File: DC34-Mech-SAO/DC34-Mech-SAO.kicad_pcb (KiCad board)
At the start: 2 copper layers, 26.8 x 37 mm, 15 parts, among them J1 Conn_01x06_Male, U1 ATTINY817-MN

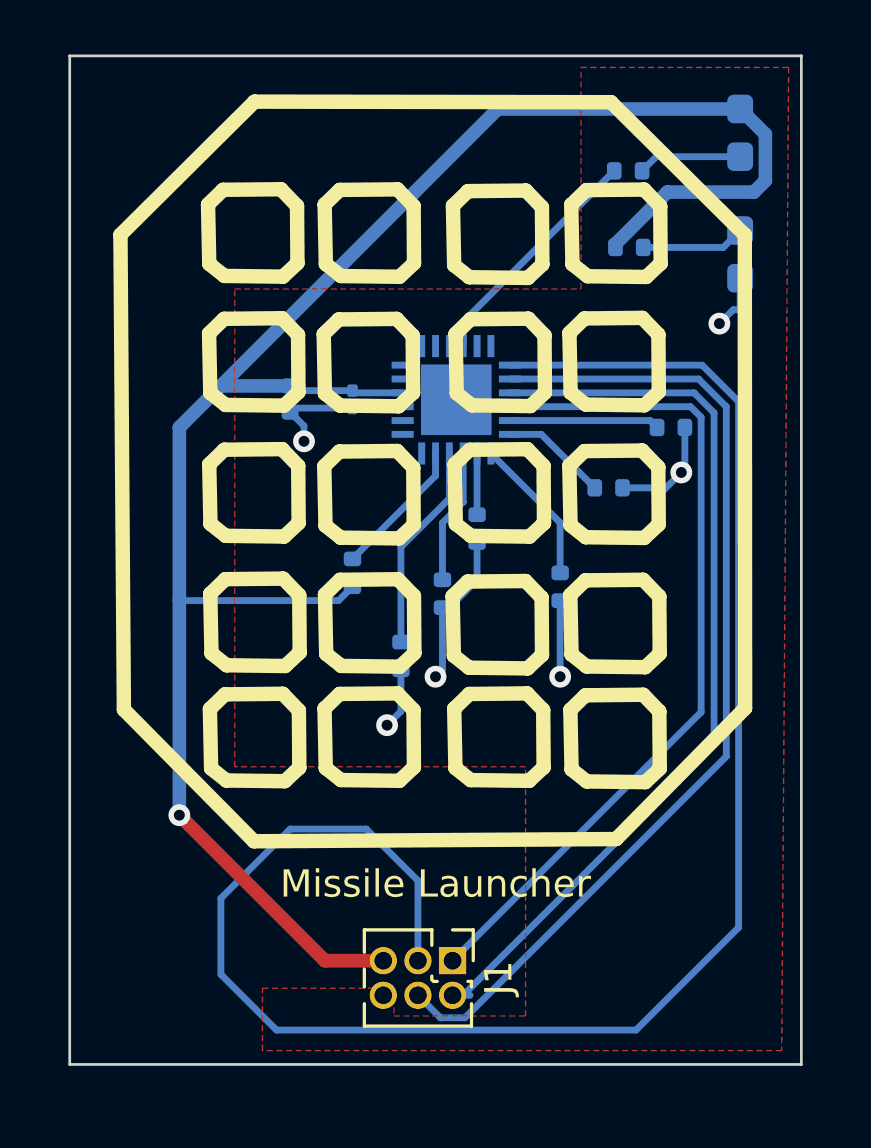
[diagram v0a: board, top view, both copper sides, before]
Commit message: Using ATTiny 816.
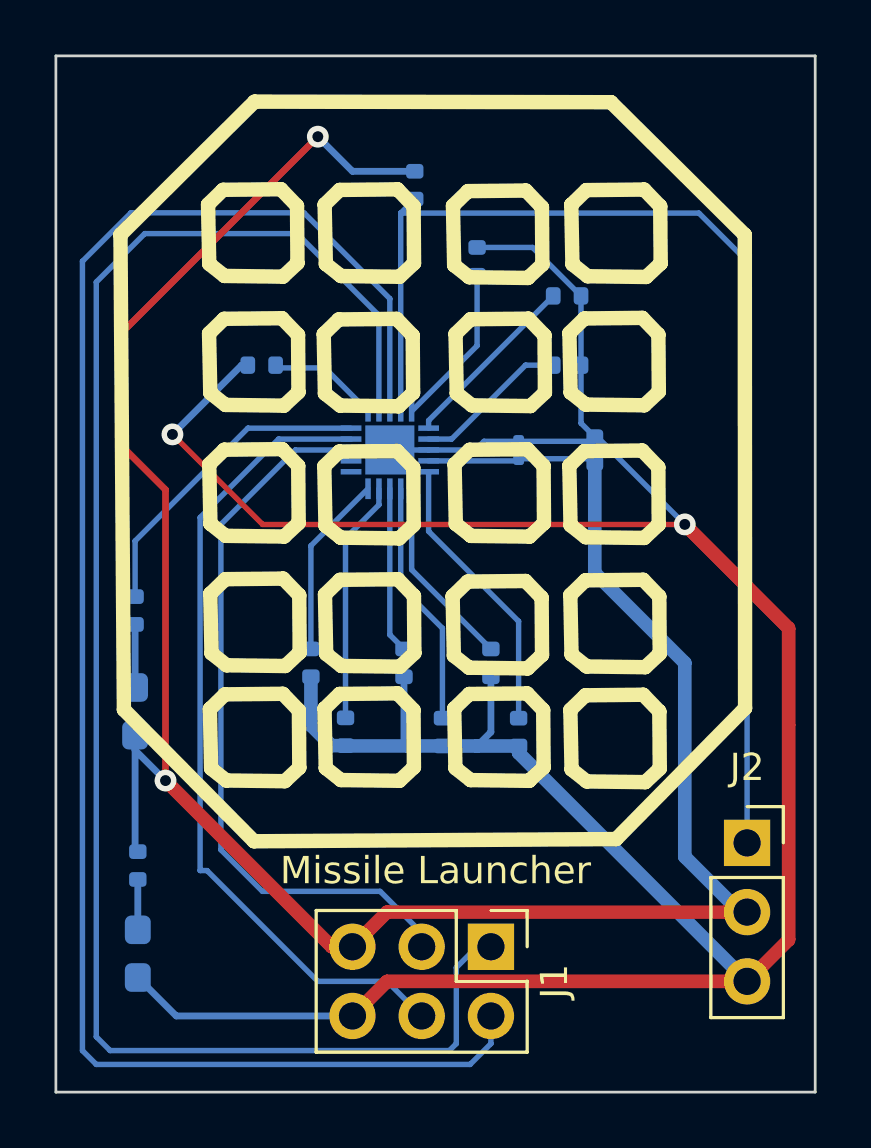
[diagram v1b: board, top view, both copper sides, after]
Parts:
- added J2: Conn_01x03_Male, Connector_PinSocket_2.54mm:PinSocket_1x03_P2.54mm_Vertical, F.Cu at (156.2, 90.9)
- added R11: 10k, Resistor_SMD:R_0402_1005Metric, B.Cu at (146.3, 69.6)
- added R12: 10k, Resistor_SMD:R_0402_1005Metric, B.Cu at (149.6, 70.9)
- added R13: 10k, Resistor_SMD:R_0402_1005Metric, B.Cu at (149.6, 73.4)
- added R7: 10k, Resistor_SMD:R_0402_1005Metric, B.Cu at (143.6, 84.3)
- J1: footprint Connector_PinHeader_1.27mm:PinHeader_2x03_P1.27mm_Vertical -> Connector_PinHeader_2.54mm:PinHeader_2x03_P2.54mm_Vertical
- U1: value ATTINY817-MN -> ATtiny816-M; footprint ATTINY817:QFN24_4X4MC_MCH -> ATTINY816:VQFN20_3X3_MCH
- moved D2 33.9 mm to (133.9, 95.0)
- moved D1 30.7 mm to (133.8, 86.1), turned to -90 degrees
- moved R2 29.0 mm to (133.9, 91.8), turned to -90 degrees
- moved R1 24.2 mm to (133.8, 82.4), turned to 90 degrees
- moved R10 15.2 mm to (138.4, 73.4), turned to 180 degrees
- moved R3 14.4 mm to (144.0, 66.8), turned to 90 degrees
- moved C1 11.3 mm to (150.6, 76.5), turned to 90 degrees
- moved R4 9.55 mm to (147.8, 86.9), turned to -90 degrees
- moved R6 7.57 mm to (145.0, 86.9)
- moved C2 6.37 mm to (147.8, 76.5), turned to 90 degrees
- moved R8 6.19 mm to (141.5, 86.9)
- moved R5 3.77 mm to (146.8, 84.3)
- moved R9 3.31 mm to (140.2, 84.3)
- moved U1 3.06 mm to (143.1, 76.5), turned to 180 degrees
- moved J1 1.50 mm to (146.8, 94.7)
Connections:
- R10 pad 1: Net-(R10-Pad1) -> IO6
- R3 pad 1: Net-(R3-Pad1) -> UPDI
- R4 pad 1: Net-(R4-Pad1) -> IO0
- R5 pad 1: Net-(R5-Pad1) -> IO1
- R6 pad 1: Net-(R6-Pad1) -> IO2
- R8 pad 1: Net-(R8-Pad1) -> IO4
- R9 pad 1: Net-(R9-Pad1) -> IO5
- U1 pad 1: unconnected-(U1-Pad1) -> IO8
- U1 pad 10: Net-(R1-Pad2) -> IO5
- U1 pad 15: GPIO2 -> Net-(R1-Pad2)
- U1 pad 16: GPIO1 -> IO6
- U1 pad 17: Net-(R10-Pad1) -> GPIO1
- U1 pad 18: Net-(R4-Pad1) -> GPIO2
- U1 pad 19: Net-(R5-Pad1) -> UPDI
- U1 pad 2: unconnected-(U1-Pad2) -> IO9
- U1 pad 20: Net-(R6-Pad1) -> IO7
- U1 pad 21: Net-(R8-Pad1) -> GND
- U1 pad 5: unconnected-(U1-Pad5) -> IO0
- U1 pad 6: unconnected-(U1-Pad6) -> IO1
- U1 pad 7: unconnected-(U1-Pad7) -> IO2
- U1 pad 8: unconnected-(U1-Pad8) -> IO3
- U1 pad 9: unconnected-(U1-Pad9) -> IO4
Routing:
- net GND: track 22.5 -> 115.9 mm, vias 6 -> 2
- net UPDI: track 0.00 -> 42.8 mm
- net SDA: track 64.4 -> 27.0 mm
- net GPIO1: track 30.9 -> 61.5 mm
- net GPIO2: track 34.0 -> 62.9 mm
- net PWR: track 72.3 -> 87.2 mm
- net IO0: track 0.00 -> 10.4 mm
- net IO2: track 0.00 -> 9.05 mm
- net IO4: track 0.00 -> 8.91 mm
- net Net-(R9-Pad1): track 7.66 -> 0.00 mm
- net IO1: track 0.00 -> 7.08 mm
- net SCL: track 36.8 -> 30.0 mm
- net IO8: track 0.00 -> 6.75 mm
- net IO5: track 0.00 -> 6.74 mm
- net IO3: track 0.00 -> 6.09 mm
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- removed copper zone on F.Cu, net GND
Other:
- board size 26.8 x 37 mm -> 27.9 x 38 mm

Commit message: change 2
added machine gun
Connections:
- R4 pad 2: GND -> PWR
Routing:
- net PWR: track 87.2 -> 94.9 mm
- net GND: track 115.9 -> 119.5 mm
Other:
- board text added: "Machine Gun"
- board text removed: "Missile Launcher"
